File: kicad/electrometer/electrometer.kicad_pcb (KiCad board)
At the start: 2 copper layers, 44.5 x 43.2 mm, 19 parts, among them J1 Screw_Terminal_01x04, J2 Screw_Terminal_01x02, J3 Conn_01x03_Male, J4 Conn_01x03_Male, M1 CD4051B, U1 LMC6082

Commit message: updated board
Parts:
- removed C2, C3: 1e-03, Capacitor_SMD:C_1206_3216Metric_Pad1.33x1.80mm_HandSolder
- removed J2: Screw_Terminal_01x02, TerminalBlock_Phoenix:TerminalBlock_Phoenix_MPT-0,5-2-2.54_1x02_P2.54mm_Horizontal
- removed J3, J4: Conn_01x03_Male, Connector_PinHeader_2.54mm:PinHeader_1x03_P2.54mm_Vertical
- removed M1: CD4051B, Package_DIP:DIP-16_W7.62mm
- removed R3: 100e+03, Resistor_SMD:R_1206_3216Metric_Pad1.30x1.75mm_HandSolder
- removed R4, R6, R7, R8: 10e+03, Resistor_SMD:R_1206_3216Metric_Pad1.30x1.75mm_HandSolder
- removed R5: 1e+03, Resistor_SMD:R_1206_3216Metric_Pad1.30x1.75mm_HandSolder
- removed the REF** at (177.8, 74.9)
- removed the REF** at (177.8, 110.5)
- added C1: 1e-03, Capacitor_SMD:C_1206_3216Metric_Pad1.33x1.80mm_HandSolder, F.Cu at (151.1, 83.8)
- added R1: 1e+03, Resistor_SMD:R_1206_3216Metric_Pad1.30x1.75mm_HandSolder, F.Cu at (147.3, 83.8)
- added R9: 1e+03, Resistor_SMD:R_1206_3216Metric_Pad1.30x1.75mm_HandSolder, F.Cu at (157.8, 97.8)
- R2: moved to F.Cu
- moved J1 29.3 mm to (148.6, 90.2)
- moved R2 19.5 mm to (157.5, 94.0)
- moved REF** 10.9 mm to (153.7, 106.7)
- moved REF** 10.2 mm to (153.7, 76.2)
- moved U1 10.2 mm to (153.7, 82.5)
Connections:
- net Net-(C2-Pad1) renamed +9V
- J1 pad 2: GND -> -9V
- J1 pad 3: Net-(C3-Pad2) -> Net-(J1-Pin_3)
- J1 pad 4: unconnected-(J1-Pad4) -> GND
- U1 pad 2: unconnected-(U1-Pad2) -> Net-(U1A--)
- U1 pad 4: Net-(C3-Pad2) -> -9V
- U1 pad 7: Net-(U1-Pad7) -> Net-(J1-Pin_3)
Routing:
- net GND: track 177.5 -> 21.9 mm
- net Net-(C3-Pad2): track 76.4 -> 0.00 mm
- net Net-(U1-Pad7): track 62.7 -> 0.00 mm
- net +9V: track 75.2 -> 25.4 mm
- net Net-(J1-Pin_3): track 0.00 -> 42.2 mm
- net Net-(U1B--): track 60.9 -> 19.6 mm
- net Net-(M1-Pad10): track 32.9 -> 0.00 mm
- net Net-(R5-Pad1): track 31.8 -> 0.00 mm
- net Net-(M1-Pad11): track 30.6 -> 0.00 mm
- net Net-(C1-Pad2): track 4.86 -> 31.5 mm
- net Net-(M1-Pad9): track 16.1 -> 0.00 mm
- net Net-(R3-Pad1): track 6.87 -> 0.00 mm
- net Net-(R4-Pad1): track 6.68 -> 0.00 mm
- net Net-(U1A--): track 0.00 -> 6.47 mm
- net -9V: track 0.00 -> 6.14 mm
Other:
- board size 44.5 x 43.2 mm -> 25.4 x 39.4 mm

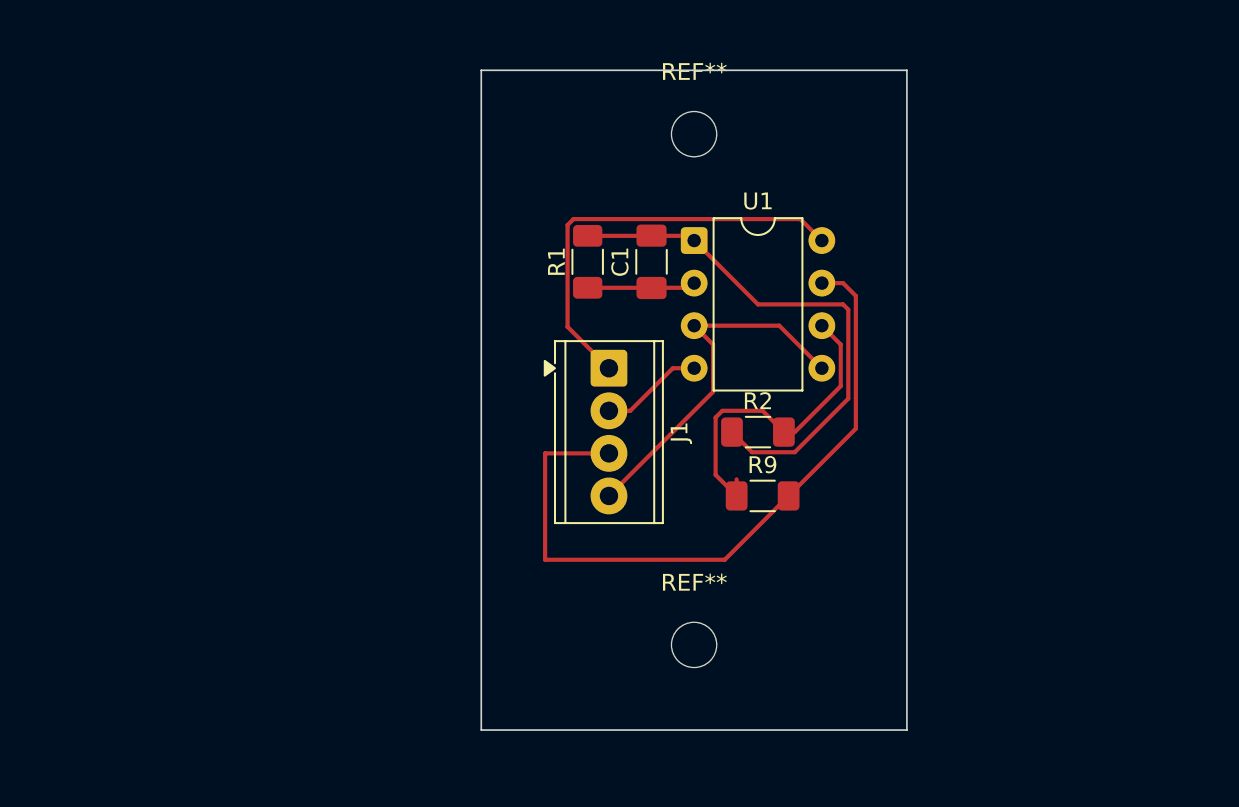
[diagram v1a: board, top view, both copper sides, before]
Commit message: moved around some kicad things. Added additional schematic for ADC and TPS60213
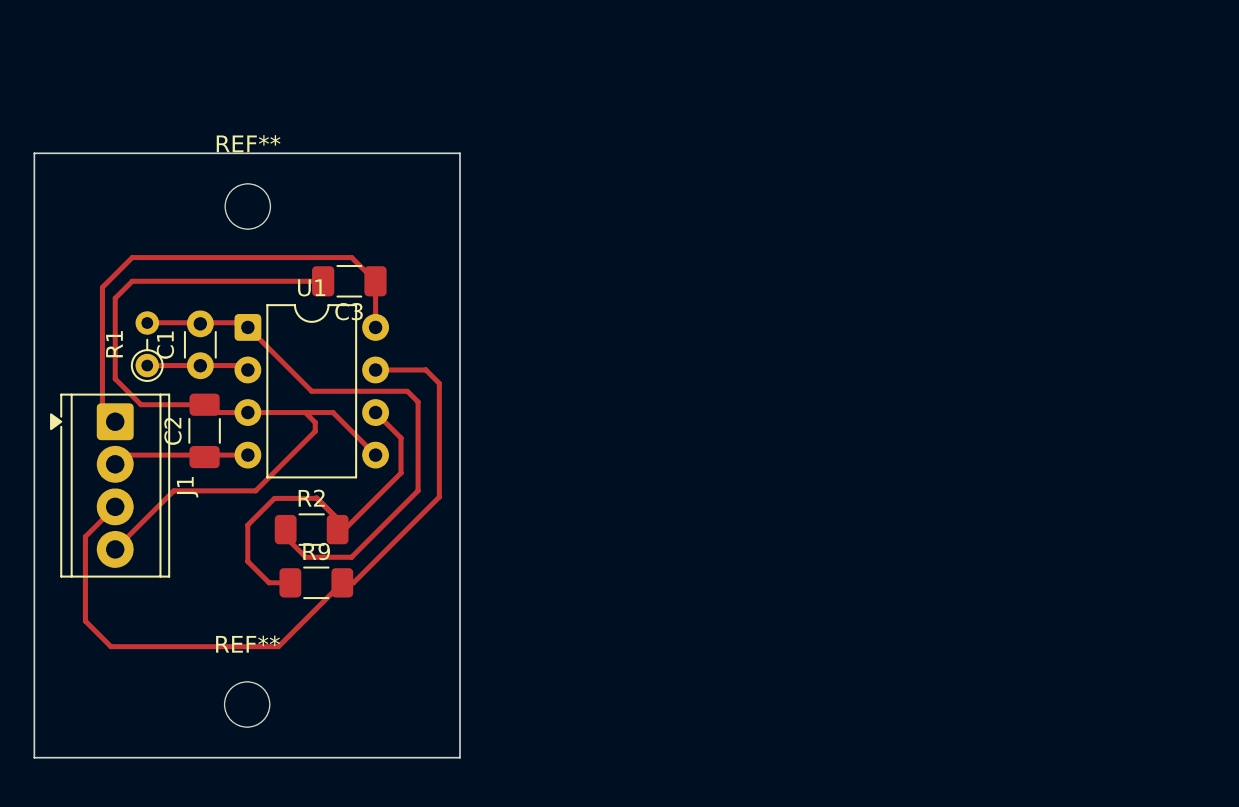
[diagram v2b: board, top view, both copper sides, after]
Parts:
- removed the REF** at (153.7, 106.7)
- removed the REF** at (153.7, 76.2)
- added C2: 1e-03, Capacitor_SMD:C_1206_3216Metric_Pad1.33x1.80mm_HandSolder, F.Cu at (124.5, 93.9)
- added C3: 1e-03, Capacitor_SMD:C_1206_3216Metric_Pad1.33x1.80mm_HandSolder, F.Cu at (133.1, 85.0)
- added REF**: MountingHole_2.7mm, MountingHole:MountingHole_2.7mm, F.Cu at (127.0, 110.2)
- added REF**: MountingHole_2.7mm, MountingHole:MountingHole_2.7mm, F.Cu at (127.0, 80.5)
- C1: footprint Capacitor_SMD:C_1206_3216Metric_Pad1.33x1.80mm_HandSolder -> Capacitor_THT:C_Disc_D3.0mm_W1.6mm_P2.50mm
- R1: footprint Resistor_SMD:R_1206_3216Metric_Pad1.30x1.75mm_HandSolder -> Resistor_THT:R_Axial_DIN0204_L3.6mm_D1.6mm_P2.54mm_Vertical
- moved J1 29.6 mm to (119.1, 93.4)
- moved C1 27.6 mm to (124.2, 90.0)
- moved R2 27.3 mm to (130.8, 99.8)
- moved R9 27.1 mm to (131.1, 103.0)
- moved U1 27.1 mm to (127.0, 87.7)
- moved R1 27.0 mm to (121.0, 90.0)
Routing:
- net GND: track 21.9 -> 51.3 mm
- net Net-(U1B--): track 19.6 -> 23.0 mm
- net +9V: track 25.4 -> 28.7 mm
- net Net-(C1-Pad2): track 31.5 -> 34.3 mm
- net -9V: track 6.14 -> 8.14 mm
- net Net-(J1-Pin_3): track 42.2 -> 43.9 mm
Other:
- board size 25.4 x 39.4 mm -> 25.4 x 36.1 mm
